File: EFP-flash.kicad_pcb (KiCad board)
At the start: 2 copper layers, 30.5 x 20.3 mm, 21 parts, among them J101 USB_B_Micro, J102 USB_C_Receptacle_USB2.0, J103 Conn_01x06, Q101 MMDT3904, SW101 SW_SPDT, U101 ESD PROTECTION, U102 TLV75533PDBV, U103 CH340C

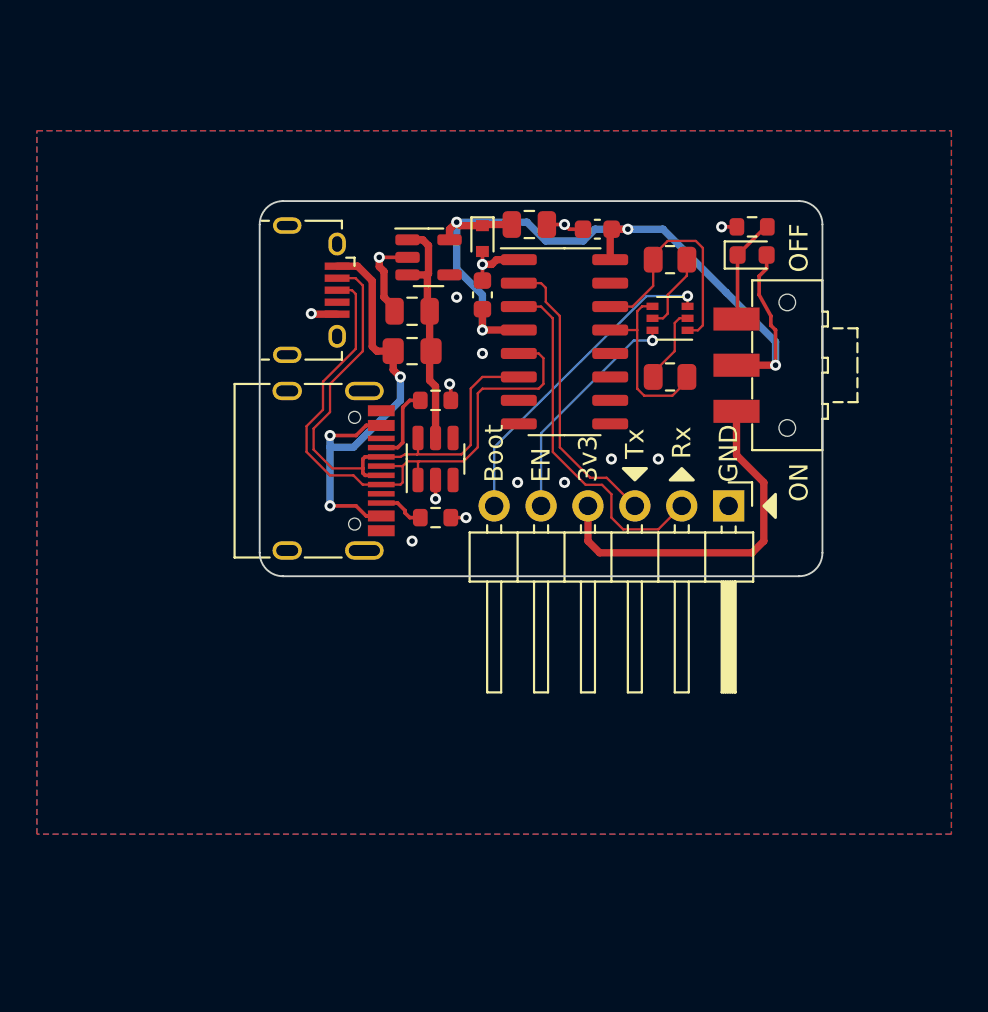
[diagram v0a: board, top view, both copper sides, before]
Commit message: Changed from right-angled to straight shape
For a lot of boards, the sideways design means the cable tends to get in
the way of things, especially cases. A straight-through format that can
be plugged in vertically would do much better.
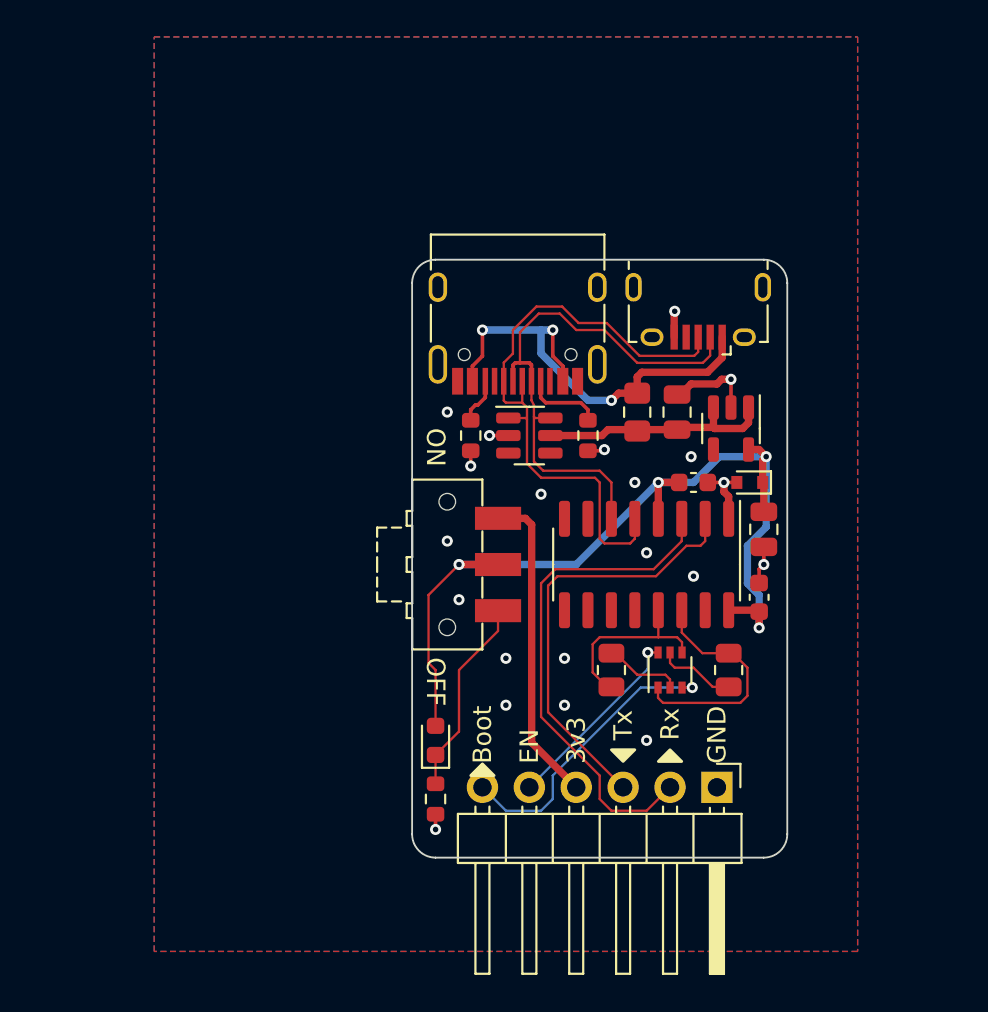
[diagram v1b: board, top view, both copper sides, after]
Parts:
- moved R105 35.4 mm to (134.0, 66.7), turned to -90 degrees
- moved D102 31.4 mm to (134.0, 63.5), turned to 90 degrees
- moved R104 22.5 mm to (149.9, 59.7), turned to 90 degrees
- moved C104 21.8 mm to (151.5, 55.8), turned to 90 degrees
- moved SW101 21.3 mm to (134.6, 54.0), turned to -90 degrees
- moved J101 21.0 mm to (148.2, 40.3), turned to 180 degrees
- moved C102 20.8 mm to (151.8, 52.1), turned to -90 degrees
- moved D101 19.6 mm to (151.0, 49.5), turned to 180 degrees
- moved Q101 19.0 mm to (146.7, 59.7), turned to 90 degrees
- moved U102 18.8 mm to (150.0, 46.6), turned to -90 degrees
- moved R103 16.2 mm to (143.5, 59.7), turned to -90 degrees
- moved C101 15.4 mm to (147.1, 45.7), turned to 90 degrees
- moved C103 15.3 mm to (148.0, 49.5), turned to 0 degrees
- moved J103 15.3 mm to (149.2, 66.0)
- moved J102 14.5 mm to (138.4, 40.0), turned to 180 degrees
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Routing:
- net /SER_RX: track 19.3 -> 27.4 mm
- net /SER_TX: track 15.9 -> 23.3 mm
- net Net-(D102-Pad1): track 5.74 -> 10.9 mm
- net +3V3: track 46.6 -> 50.6 mm
- net /3v3_{SW}: track 19.6 -> 17.2 mm
- net /EN: track 12.6 -> 10.5 mm
- net /Boot: track 17.6 -> 16.0 mm
- net GND: vias 15 -> 21
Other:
- board size 30.5 x 20.3 mm -> 20.3 x 32.4 mm

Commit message: Add 2nd indicator LED
- The first one is linked to the switch, and indicates when the switch
  is closed, linking the 3v3 nets together.
- The second one is linked directly to the 3v3 pin on the programmer. It
  will also turn on when the target board has its own power source.
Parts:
- added D103: GREEN, LED_SMD:LED_0603_1608Metric, F.Cu at (151.8, 63.5)
- added R106: 10kΩ, Resistor_SMD:R_0603_1608Metric, F.Cu at (151.8, 66.7)
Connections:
- SW101 pad 1: /3v3_{SW} -> Net-(D102-Pad1)
- SW101 pad 3: Net-(D102-Pad1) -> /3v3_{SW}
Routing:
- net /3v3_{SW}: track 17.2 -> 27.8 mm, vias 0 -> 1
- net Net-(D102-Pad1): track 10.9 -> 18.6 mm
- net Net-(D103-Pad1): track 0.00 -> 1.56 mm
- net GND: track 15.5 -> 14.7 mm, vias 21 -> 19
- net +3V3: track 50.6 -> 51.3 mm, vias 4 -> 5

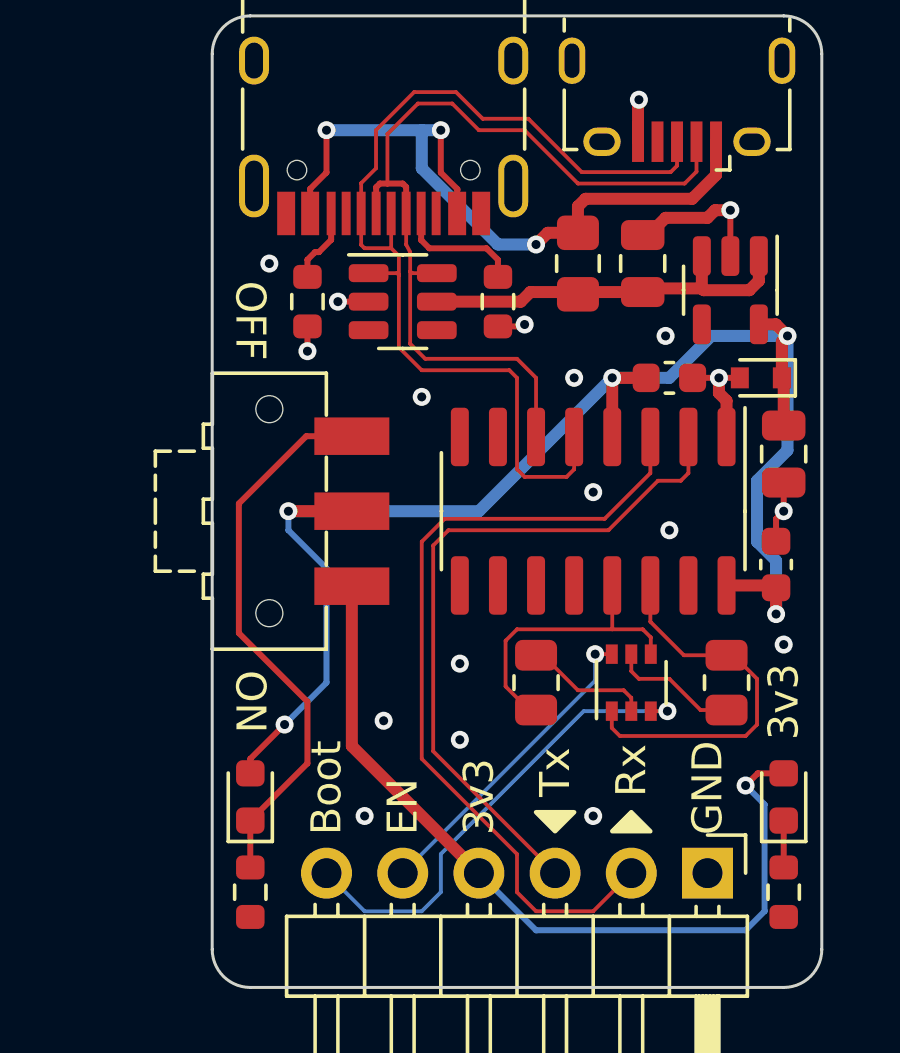
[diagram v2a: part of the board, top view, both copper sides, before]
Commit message: Convert to 7.0 format, fix DRC errors
Opened and saved with KiCAD 7.0

Fix a few unconnected components. Adjusted DRC violation severities to
ignore silkscreen over board edge (because they're usually on purpose
and don't help track down errors).
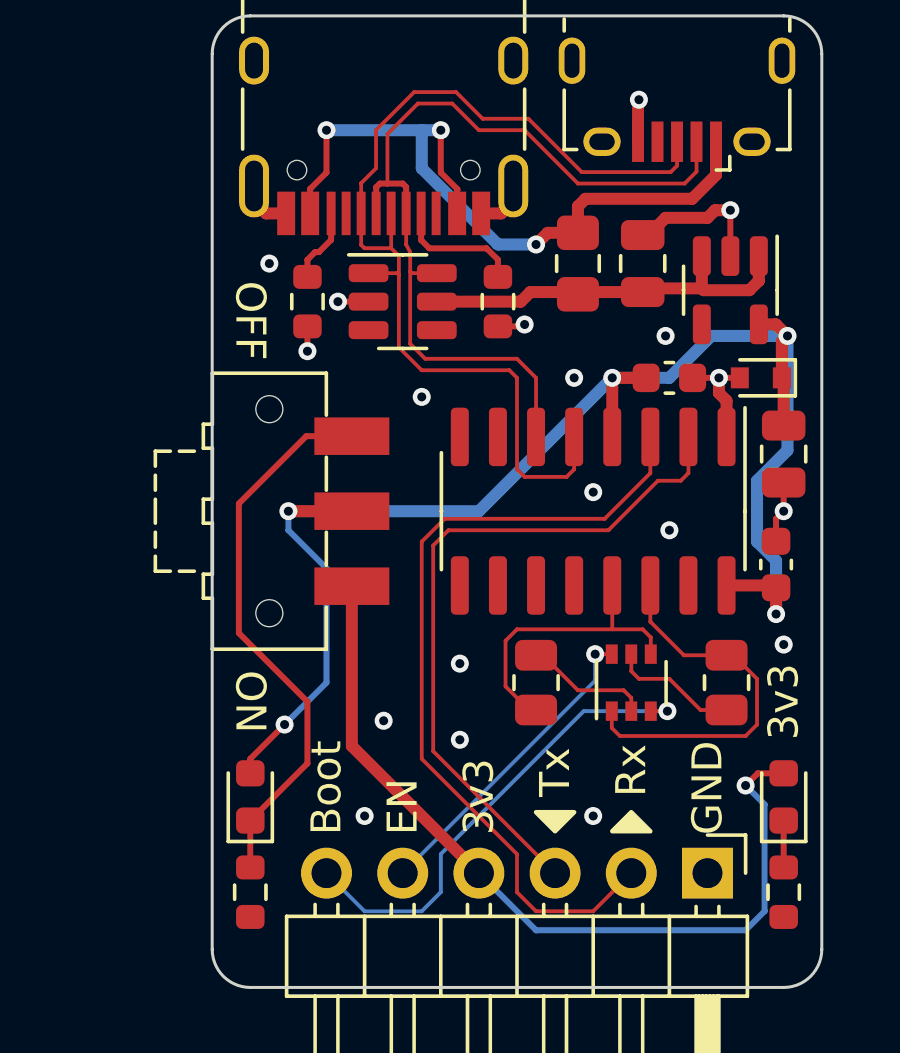
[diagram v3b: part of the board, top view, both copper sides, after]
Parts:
- moved LOGO101 3.52 mm to (147.3, 45.7)
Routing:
- net GND: track 14.7 -> 18.2 mm
